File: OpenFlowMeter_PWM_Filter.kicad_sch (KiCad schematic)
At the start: 10 parts, among them U3 LT1492

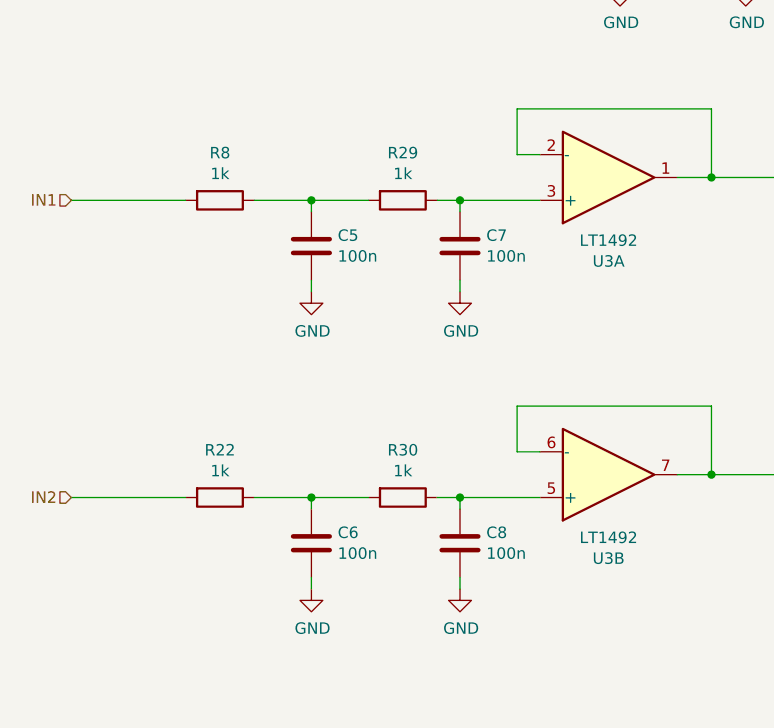
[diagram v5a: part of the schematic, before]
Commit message: included values from simulation
added values to those components, which did not had one
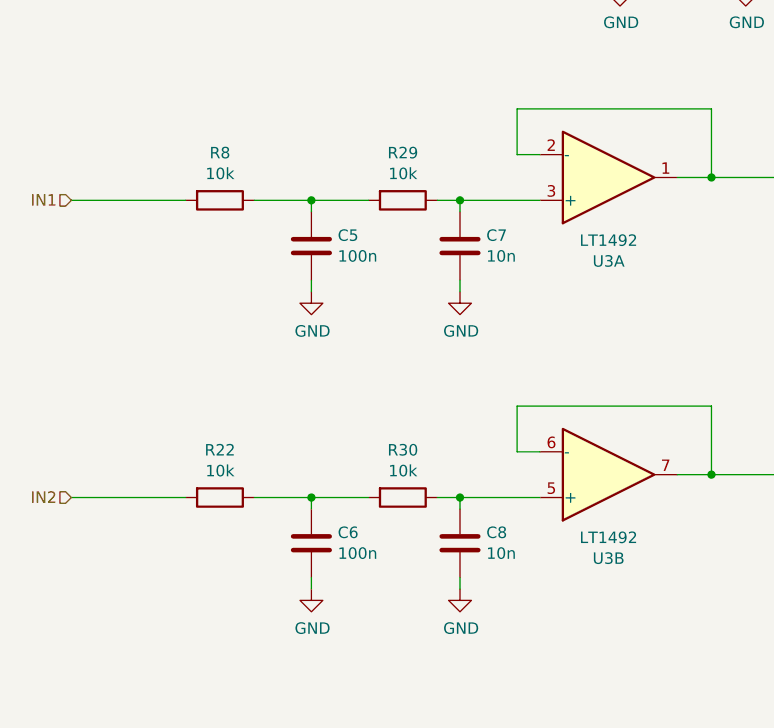
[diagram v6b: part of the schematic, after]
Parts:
- C7, C8: value 100n -> 10n
- R22, R29, R30, R8: value 1k -> 10k
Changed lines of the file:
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@@
     (in_bom yes) (on_board yes)
     (property "Reference" "R8" (id 0) (at 104.14 88.7222 90))
-    (property "Value" "1k" (id 1) (at 104.14 91.0336 90))
+    (property "Value" "10k" (id 1) (at 104.14 91.0336 90))
     (property "Footprint" "Resistor_SMD:R_0603_1608Metric" (id 2) (at 104.14 92.202 90)
       (effects (font (size 1.27 1.27)) hide)
@@
     (in_bom yes) (on_board yes)
     (property "Reference" "R29" (id 0) (at 124.46 88.7222 90))
-    (property "Value" "1k" (id 1) (at 124.46 91.0336 90))
+    (property "Value" "10k" (id 1) (at 124.46 91.0336 90))
     (property "Footprint" "Resistor_SMD:R_0603_1608Metric" (id 2) (at 124.46 92.202 90)
       (effects (font (size 1.27 1.27)) hide)
@@
       (effects (font (size 1.27 1.27)) (justify left))
     )
-    (property "Value" "100n" (id 1) (at 133.731 100.203 0)
+    (property "Value" "10n" (id 1) (at 133.731 100.203 0)
       (effects (font (size 1.27 1.27)) (justify left))
     )
@@
     (in_bom yes) (on_board yes)
     (property "Reference" "R22" (id 0) (at 104.14 121.7422 90))
-    (property "Value" "1k" (id 1) (at 104.14 124.0536 90))
+    (property "Value" "10k" (id 1) (at 104.14 124.0536 90))
     (property "Footprint" "Resistor_SMD:R_0603_1608Metric" (id 2) (at 104.14 125.222 90)
       (effects (font (size 1.27 1.27)) hide)
@@
     (in_bom yes) (on_board yes)
     (property "Reference" "R30" (id 0) (at 124.46 121.7422 90))
-    (property "Value" "1k" (id 1) (at 124.46 124.0536 90))
+    (property "Value" "10k" (id 1) (at 124.46 124.0536 90))
     (property "Footprint" "Resistor_SMD:R_0603_1608Metric" (id 2) (at 124.46 125.222 90)
       (effects (font (size 1.27 1.27)) hide)
@@
       (effects (font (size 1.27 1.27)) (justify left))
     )
-    (property "Value" "100n" (id 1) (at 133.731 133.223 0)
+    (property "Value" "10n" (id 1) (at 133.731 133.223 0)
       (effects (font (size 1.27 1.27)) (justify left))
     )

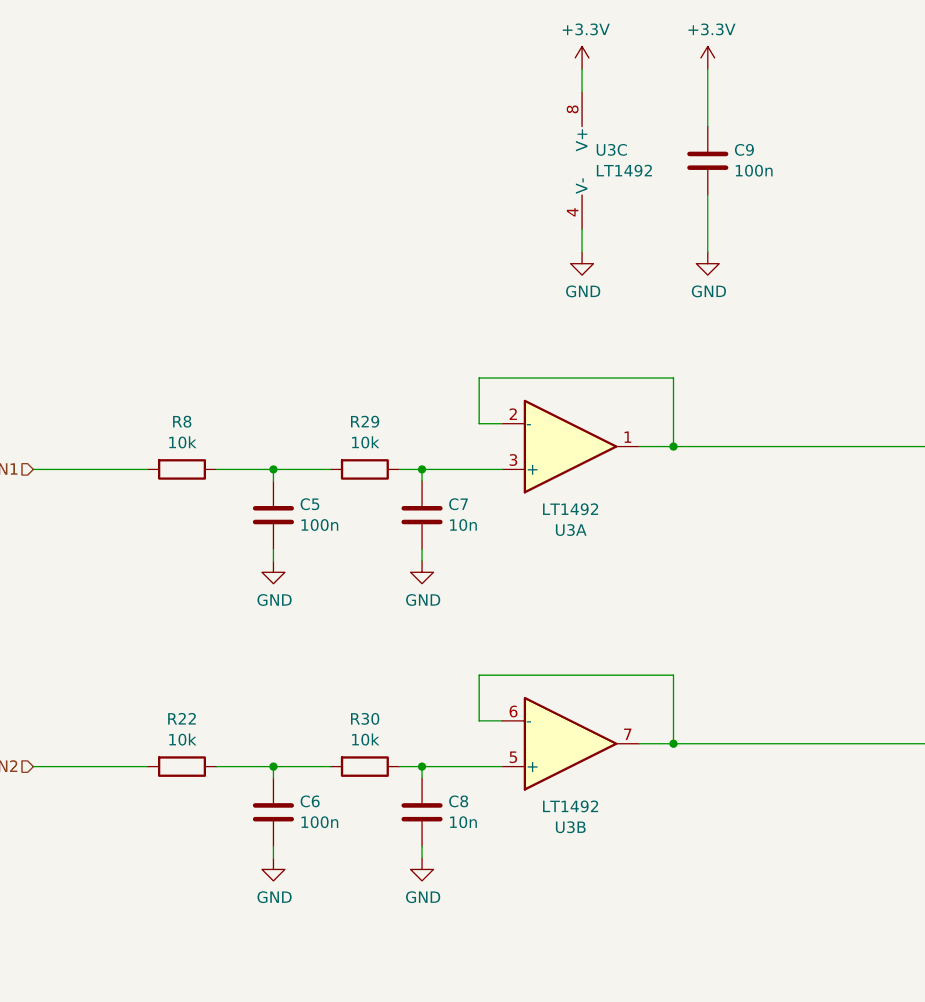
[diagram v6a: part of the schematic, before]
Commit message: inlcuded switching gain amplifier
aim is to increase the voltage and current reading for small currents and voltages.
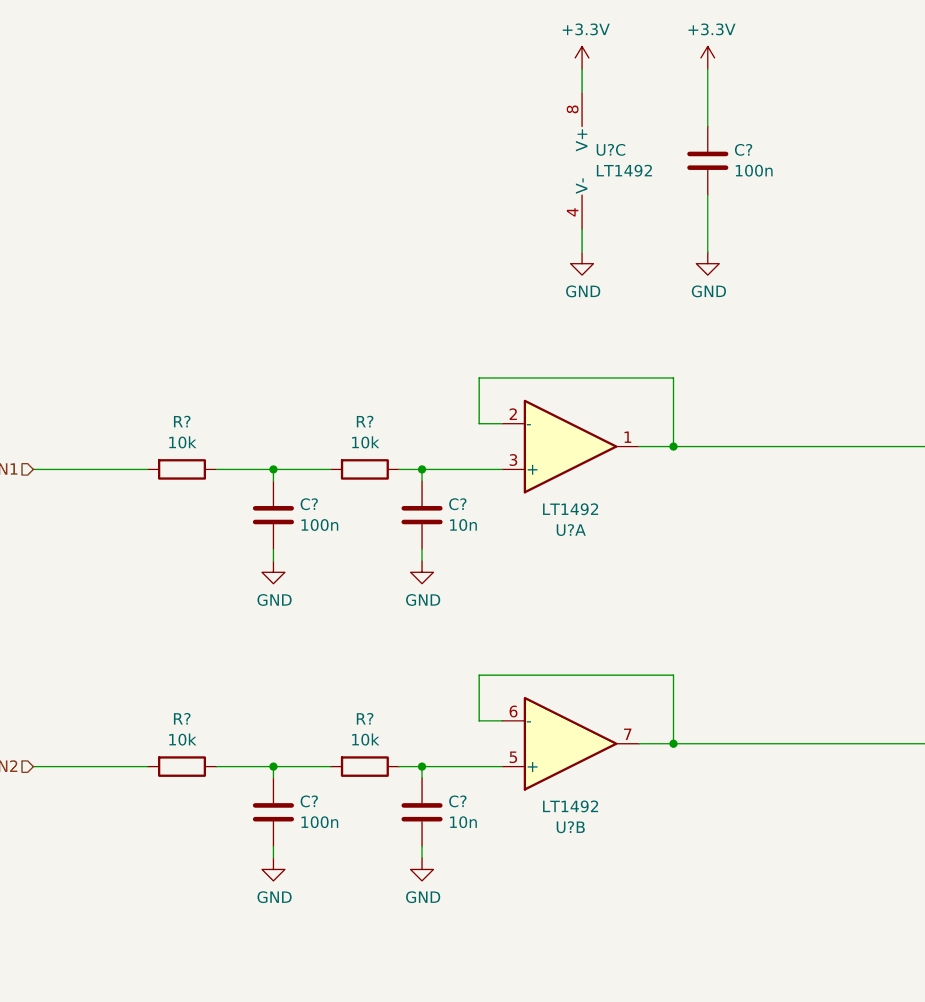
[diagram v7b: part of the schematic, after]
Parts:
- renumbered C9 to C?, C5 to C?, C7 to C?, C6 to C?, C8 to C?, R8 to R?, R29 to R?, R22 to R?, R30 to R?, U3 to U?
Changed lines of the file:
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@@
   (symbol (lib_id "Amplifier_Operational:LT1492") (at 147.32 91.44 0) (mirror x) (unit 1)
     (in_bom yes) (on_board yes)
-    (property "Reference" "U3" (id 0) (at 147.32 100.7618 0))
+    (property "Reference" "U?" (id 0) (at 147.32 100.7618 0))
     (property "Value" "LT1492" (id 1) (at 147.32 98.4504 0))
     (property "Footprint" "Package_SO:SOIC-8_3.9x4.9mm_P1.27mm" (id 2) (at 147.32 91.44 0)
@@
   (symbol (lib_id "Amplifier_Operational:LT1492") (at 151.13 59.69 0) (unit 3)
     (in_bom yes) (on_board yes)
-    (property "Reference" "U3" (id 0) (at 150.0632 58.5216 0)
+    (property "Reference" "U?" (id 0) (at 150.0632 58.5216 0)
       (effects (font (size 1.27 1.27)) (justify left))
     )
@@
   (symbol (lib_id "Device:C") (at 162.56 59.69 0) (unit 1)
     (in_bom yes) (on_board yes)
-    (property "Reference" "C9" (id 0) (at 165.481 58.5216 0)
+    (property "Reference" "C?" (id 0) (at 165.481 58.5216 0)
       (effects (font (size 1.27 1.27)) (justify left))
     )
@@
   (symbol (lib_id "Amplifier_Operational:LT1492") (at 147.32 124.46 0) (mirror x) (unit 2)
     (in_bom yes) (on_board yes)
-    (property "Reference" "U3" (id 0) (at 147.32 133.7818 0))
+    (property "Reference" "U?" (id 0) (at 147.32 133.7818 0))
     (property "Value" "LT1492" (id 1) (at 147.32 131.4704 0))
     (property "Footprint" "Package_SO:SOIC-8_3.9x4.9mm_P1.27mm" (id 2) (at 147.32 124.46 0)
@@
   (symbol (lib_id "Device:R") (at 104.14 93.98 270) (unit 1)
     (in_bom yes) (on_board yes)
-    (property "Reference" "R8" (id 0) (at 104.14 88.7222 90))
+    (property "Reference" "R?" (id 0) (at 104.14 88.7222 90))
     (property "Value" "10k" (id 1) (at 104.14 91.0336 90))
     (property "Footprint" "Resistor_SMD:R_0603_1608Metric" (id 2) (at 104.14 92.202 90)
@@
   (symbol (lib_id "Device:R") (at 124.46 93.98 270) (unit 1)
     (in_bom yes) (on_board yes)
-    (property "Reference" "R29" (id 0) (at 124.46 88.7222 90))
+    (property "Reference" "R?" (id 0) (at 124.46 88.7222 90))
     (property "Value" "10k" (id 1) (at 124.46 91.0336 90))
     (property "Footprint" "Resistor_SMD:R_0603_1608Metric" (id 2) (at 124.46 92.202 90)
@@
   (symbol (lib_id "Device:C") (at 114.3 99.06 0) (unit 1)
     (in_bom yes) (on_board yes)
-    (property "Reference" "C5" (id 0) (at 117.221 97.8916 0)
+    (property "Reference" "C?" (id 0) (at 117.221 97.8916 0)
       (effects (font (size 1.27 1.27)) (justify left))
     )
@@
   (symbol (lib_id "Device:C") (at 130.81 99.06 0) (unit 1)
     (in_bom yes) (on_board yes)
-    (property "Reference" "C7" (id 0) (at 133.731 97.8916 0)
+    (property "Reference" "C?" (id 0) (at 133.731 97.8916 0)
       (effects (font (size 1.27 1.27)) (justify left))
     )
@@
   (symbol (lib_id "Device:R") (at 104.14 127 270) (unit 1)
     (in_bom yes) (on_board yes)
-    (property "Reference" "R22" (id 0) (at 104.14 121.7422 90))
+    (property "Reference" "R?" (id 0) (at 104.14 121.7422 90))
     (property "Value" "10k" (id 1) (at 104.14 124.0536 90))
     (property "Footprint" "Resistor_SMD:R_0603_1608Metric" (id 2) (at 104.14 125.222 90)
@@
   (symbol (lib_id "Device:R") (at 124.46 127 270) (unit 1)
     (in_bom yes) (on_board yes)
-    (property "Reference" "R30" (id 0) (at 124.46 121.7422 90))
+    (property "Reference" "R?" (id 0) (at 124.46 121.7422 90))
     (property "Value" "10k" (id 1) (at 124.46 124.0536 90))
     (property "Footprint" "Resistor_SMD:R_0603_1608Metric" (id 2) (at 124.46 125.222 90)
@@
   (symbol (lib_id "Device:C") (at 114.3 132.08 0) (unit 1)
     (in_bom yes) (on_board yes)
-    (property "Reference" "C6" (id 0) (at 117.221 130.9116 0)
+    (property "Reference" "C?" (id 0) (at 117.221 130.9116 0)
       (effects (font (size 1.27 1.27)) (justify left))
     )
@@
   (symbol (lib_id "Device:C") (at 130.81 132.08 0) (unit 1)
     (in_bom yes) (on_board yes)
-    (property "Reference" "C8" (id 0) (at 133.731 130.9116 0)
-      (effects (font (size 1.27 1.27)) (justify left))
-    )
+    (property "Reference" "C?" (id 0) (at 133.731 130.9116 0)
+      (effects (font (size 1.27 1.27)) (justify left))
+    )

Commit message: starting finishing the layout
some distances are not 100% and some components are too close together
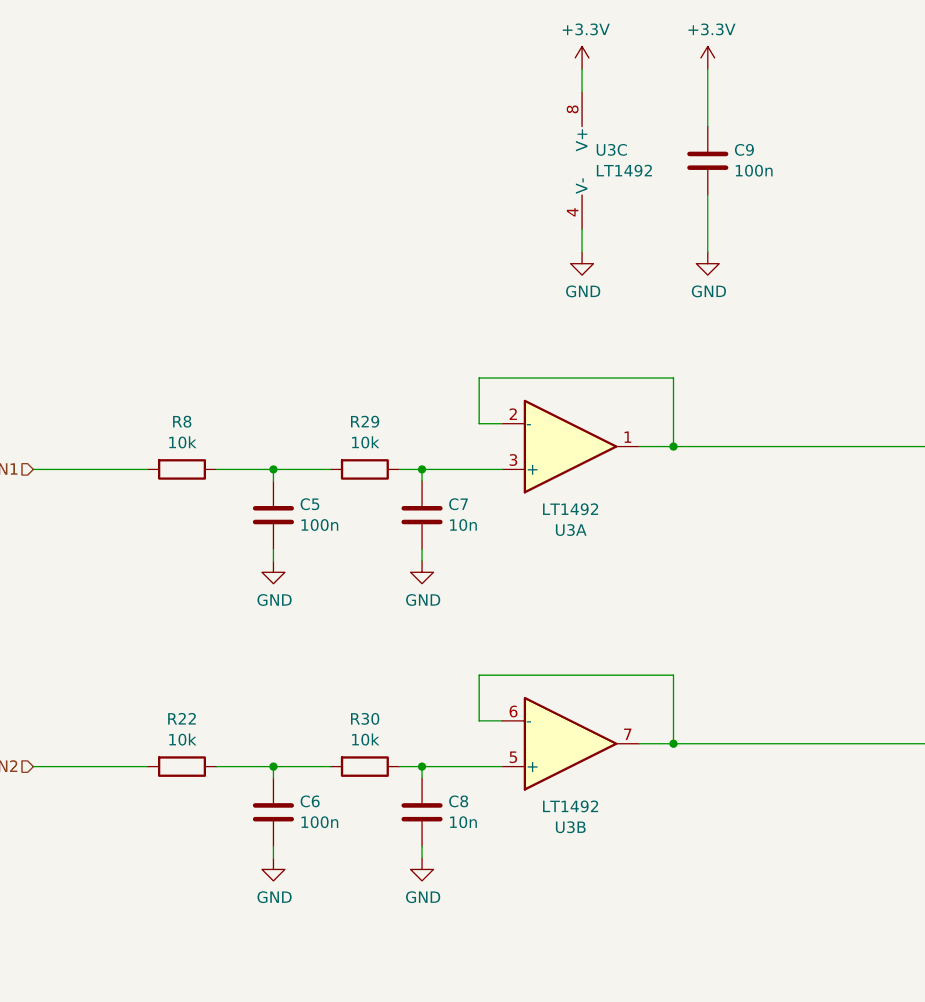
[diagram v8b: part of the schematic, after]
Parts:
- gave numbers to parts that had none: 10
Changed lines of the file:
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@@
   (symbol (lib_id "Amplifier_Operational:LT1492") (at 147.32 91.44 0) (mirror x) (unit 1)
     (in_bom yes) (on_board yes)
-    (property "Reference" "U?" (id 0) (at 147.32 100.7618 0))
+    (property "Reference" "U3" (id 0) (at 147.32 100.7618 0))
     (property "Value" "LT1492" (id 1) (at 147.32 98.4504 0))
     (property "Footprint" "Package_SO:SOIC-8_3.9x4.9mm_P1.27mm" (id 2) (at 147.32 91.44 0)
@@
   (symbol (lib_id "Amplifier_Operational:LT1492") (at 151.13 59.69 0) (unit 3)
     (in_bom yes) (on_board yes)
-    (property "Reference" "U?" (id 0) (at 150.0632 58.5216 0)
+    (property "Reference" "U3" (id 0) (at 150.0632 58.5216 0)
       (effects (font (size 1.27 1.27)) (justify left))
     )
@@
   (symbol (lib_id "Device:C") (at 162.56 59.69 0) (unit 1)
     (in_bom yes) (on_board yes)
-    (property "Reference" "C?" (id 0) (at 165.481 58.5216 0)
+    (property "Reference" "C9" (id 0) (at 165.481 58.5216 0)
       (effects (font (size 1.27 1.27)) (justify left))
     )
@@
   (symbol (lib_id "Amplifier_Operational:LT1492") (at 147.32 124.46 0) (mirror x) (unit 2)
     (in_bom yes) (on_board yes)
-    (property "Reference" "U?" (id 0) (at 147.32 133.7818 0))
+    (property "Reference" "U3" (id 0) (at 147.32 133.7818 0))
     (property "Value" "LT1492" (id 1) (at 147.32 131.4704 0))
     (property "Footprint" "Package_SO:SOIC-8_3.9x4.9mm_P1.27mm" (id 2) (at 147.32 124.46 0)
@@
   (symbol (lib_id "Device:R") (at 104.14 93.98 270) (unit 1)
     (in_bom yes) (on_board yes)
-    (property "Reference" "R?" (id 0) (at 104.14 88.7222 90))
+    (property "Reference" "R8" (id 0) (at 104.14 88.7222 90))
     (property "Value" "10k" (id 1) (at 104.14 91.0336 90))
     (property "Footprint" "Resistor_SMD:R_0603_1608Metric" (id 2) (at 104.14 92.202 90)
@@
   (symbol (lib_id "Device:R") (at 124.46 93.98 270) (unit 1)
     (in_bom yes) (on_board yes)
-    (property "Reference" "R?" (id 0) (at 124.46 88.7222 90))
+    (property "Reference" "R29" (id 0) (at 124.46 88.7222 90))
     (property "Value" "10k" (id 1) (at 124.46 91.0336 90))
     (property "Footprint" "Resistor_SMD:R_0603_1608Metric" (id 2) (at 124.46 92.202 90)
@@
   (symbol (lib_id "Device:C") (at 114.3 99.06 0) (unit 1)
     (in_bom yes) (on_board yes)
-    (property "Reference" "C?" (id 0) (at 117.221 97.8916 0)
+    (property "Reference" "C5" (id 0) (at 117.221 97.8916 0)
       (effects (font (size 1.27 1.27)) (justify left))
     )
@@
   (symbol (lib_id "Device:C") (at 130.81 99.06 0) (unit 1)
     (in_bom yes) (on_board yes)
-    (property "Reference" "C?" (id 0) (at 133.731 97.8916 0)
+    (property "Reference" "C7" (id 0) (at 133.731 97.8916 0)
       (effects (font (size 1.27 1.27)) (justify left))
     )
@@
   (symbol (lib_id "Device:R") (at 104.14 127 270) (unit 1)
     (in_bom yes) (on_board yes)
-    (property "Reference" "R?" (id 0) (at 104.14 121.7422 90))
+    (property "Reference" "R22" (id 0) (at 104.14 121.7422 90))
     (property "Value" "10k" (id 1) (at 104.14 124.0536 90))
     (property "Footprint" "Resistor_SMD:R_0603_1608Metric" (id 2) (at 104.14 125.222 90)
@@
   (symbol (lib_id "Device:R") (at 124.46 127 270) (unit 1)
     (in_bom yes) (on_board yes)
-    (property "Reference" "R?" (id 0) (at 124.46 121.7422 90))
+    (property "Reference" "R30" (id 0) (at 124.46 121.7422 90))
     (property "Value" "10k" (id 1) (at 124.46 124.0536 90))
     (property "Footprint" "Resistor_SMD:R_0603_1608Metric" (id 2) (at 124.46 125.222 90)
@@
   (symbol (lib_id "Device:C") (at 114.3 132.08 0) (unit 1)
     (in_bom yes) (on_board yes)
-    (property "Reference" "C?" (id 0) (at 117.221 130.9116 0)
+    (property "Reference" "C6" (id 0) (at 117.221 130.9116 0)
       (effects (font (size 1.27 1.27)) (justify left))
     )
@@
   (symbol (lib_id "Device:C") (at 130.81 132.08 0) (unit 1)
     (in_bom yes) (on_board yes)
-    (property "Reference" "C?" (id 0) (at 133.731 130.9116 0)
-      (effects (font (size 1.27 1.27)) (justify left))
-    )
+    (property "Reference" "C8" (id 0) (at 133.731 130.9116 0)
+      (effects (font (size 1.27 1.27)) (justify left))
+    )
